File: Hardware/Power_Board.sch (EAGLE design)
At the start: 40 parts, among them K1 E3206S, K2 E3206S, K3 E3206S, K4 E3206S, K5 E3206S, K6 E3206S, Q1 BD135, Q2 BD135, Q3 BD135, Q4 BD135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

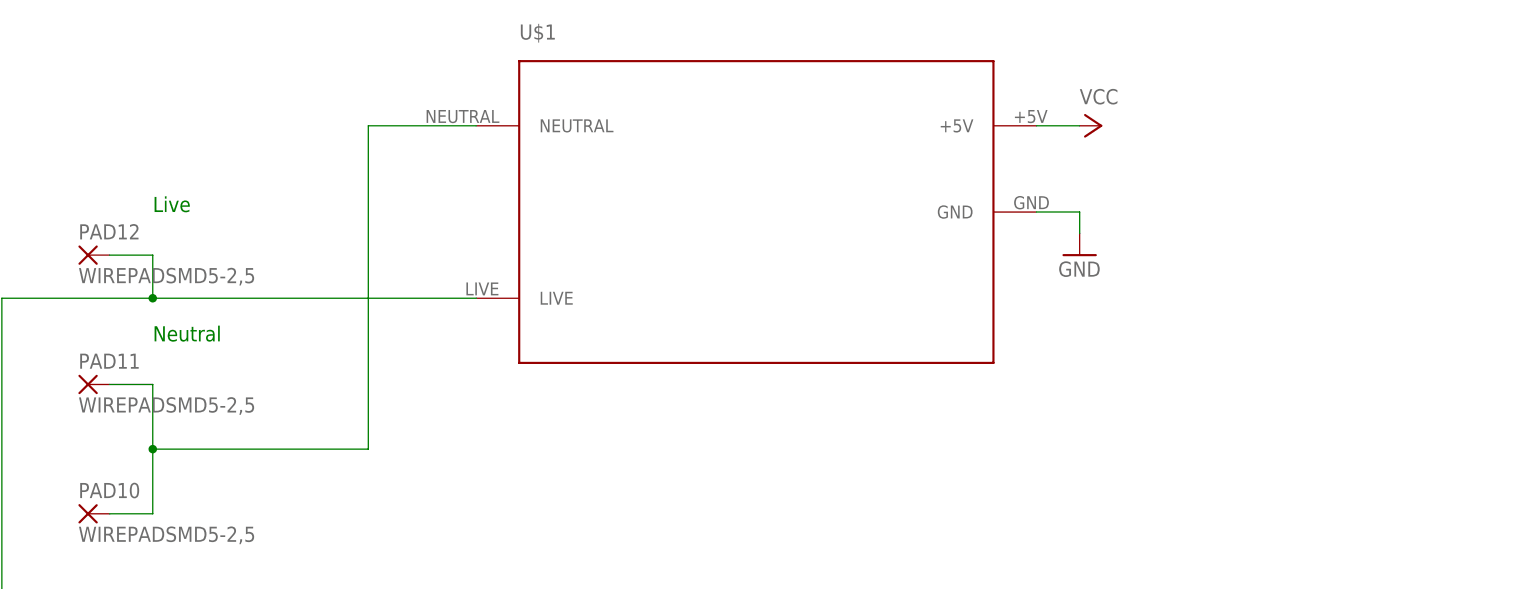
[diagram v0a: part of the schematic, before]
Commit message: Added a fuse to the power board and made PCB routes thicker.
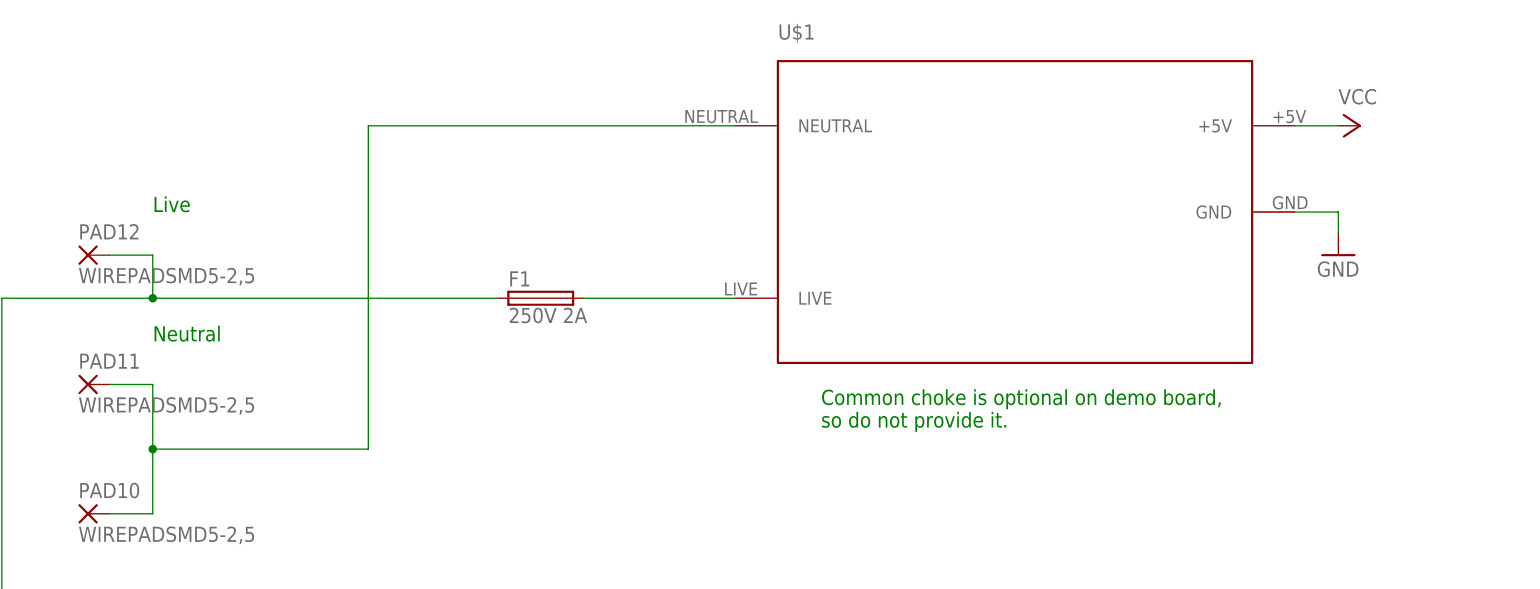
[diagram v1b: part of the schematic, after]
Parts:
- added F1: 250V 2A, fuse:GSH15
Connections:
- new net N$29: F1.2, U$1.LIVE
- net N$10: now also F1.1; no longer U$1.LIVE
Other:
- note added: "Common choke is optional on demo board, so do not provide it."
- moved on the sheet: U$1
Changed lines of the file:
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@@
 <?xml version="1.0" encoding="utf-8"?>
 <!DOCTYPE eagle SYSTEM "eagle.dtd">
-<eagle version="8.3.1">
+<eagle version="8.4.1">
 <drawing>
 <settings>
@@
 <setting verticaltext="down"/>
 </settings>
-<grid distance="0.1" unitdist="inch" unit="inch" style="dots" multiple="1" display="yes" altdistance="0.01" altunitdist="inch" altunit="inch"/>
+<grid distance="0.1" unitdist="inch" unit="inch" style="lines" multiple="1" display="no" altdistance="0.01" altunitdist="inch" altunit="inch"/>
 <layers>
 <layer number="1" name="Top" color="4" fill="1" visible="no" active="no"/>
@@
 <part name="P+1" library="supply1" deviceset="VCC" device=""/>
 <part name="X1" library="con-wago-508" deviceset="W237-02P" device="" value="230V"/>
+<part name="F1" library="fuse" deviceset="GSH15" device="" value="250V 2A"/>
 </parts>
 <sheets>
@@
 <text x="198.12" y="294.64" size="1.778" layer="91">Live</text>
 <text x="180.34" y="294.64" size="1.778" layer="91">Neutral</text>
+<text x="43.18" y="289.56" size="1.778" layer="91">Common choke is optional on demo board,
+so do not provide it.</text>
 </plain>
 <instances>
@@
 <instance part="R5" gate="G$1" x="297.18" y="195.58"/>
 <instance part="R6" gate="G$1" x="297.18" y="165.1"/>
-<instance part="U$1" gate="G$1" x="35.56" y="314.96"/>
-<instance part="GND4" gate="1" x="73.66" y="309.88"/>
-<instance part="P+1" gate="VCC" x="76.2" y="325.12" rot="R270"/>
+<instance part="U$1" gate="G$1" x="66.04" y="314.96"/>
+<instance part="GND4" gate="1" x="104.14" y="309.88"/>
+<instance part="P+1" gate="VCC" x="106.68" y="325.12" rot="R270"/>
 <instance part="X1" gate="-1" x="195.58" y="294.64" smashed="yes" rot="R270">
 <attribute name="NAME" x="196.469" y="295.91" size="1.778" layer="95" rot="R90"/>
@@
 <attribute name="NAME" x="191.389" y="295.91" size="1.778" layer="95" rot="R90"/>
 </instance>
+<instance part="F1" gate="1" x="10.16" y="304.8"/>
 </instances>
 <busses>
@@
 <segment>
 <pinref part="U$1" gate="G$1" pin="GND"/>
-<wire x1="68.58" y1="314.96" x2="73.66" y2="314.96" width="0.1524" layer="91"/>
+<wire x1="99.06" y1="314.96" x2="104.14" y2="314.96" width="0.1524" layer="91"/>
 <pinref part="GND4" gate="1" pin="GND"/>
-<wire x1="73.66" y1="314.96" x2="73.66" y2="312.42" width="0.1524" layer="91"/>
+<wire x1="104.14" y1="314.96" x2="104.14" y2="312.42" width="0.1524" layer="91"/>
 </segment>
 </net>
@@
 <pinref part="U$1" gate="G$1" pin="+5V"/>
 <pinref part="P+1" gate="VCC" pin="VCC"/>
-<wire x1="68.58" y1="325.12" x2="73.66" y2="325.12" width="0.1524" layer="91"/>
+<wire x1="99.06" y1="325.12" x2="104.14" y2="325.12" width="0.1524" layer="91"/>
 </segment>
 </net>
@@
 <wire x1="-5.08" y1="243.84" x2="-53.34" y2="243.84" width="0.1524" layer="91"/>
 <junction x="-53.34" y="243.84"/>
-<wire x1="-35.56" y1="304.8" x2="2.54" y2="304.8" width="0.1524" layer="91"/>
+<pinref part="F1" gate="1" pin="1"/>
+<wire x1="-35.56" y1="304.8" x2="5.08" y2="304.8" width="0.1524" layer="91"/>
 <junction x="-35.56" y="304.8"/>
-<pinref part="U$1" gate="G$1" pin="LIVE"/>
 </segment>
 </net>
@@
 <segment>
 <pinref part="U$1" gate="G$1" pin="NEUTRAL"/>
-<wire x1="-10.16" y1="325.12" x2="2.54" y2="325.12" width="0.1524" layer="91"/>
+<wire x1="-10.16" y1="325.12" x2="33.02" y2="325.12" width="0.1524" layer="91"/>
 <wire x1="-10.16" y1="287.02" x2="-10.16" y2="325.12" width="0.1524" layer="91"/>
 <pinref part="PAD10" gate="G$1" pin="P"/>
@@
 </segment>
 </net>
+<net name="N$29" class="1">
+<segment>
+<pinref part="F1" gate="1" pin="2"/>
+<pinref part="U$1" gate="G$1" pin="LIVE"/>
+<wire x1="15.24" y1="304.8" x2="33.02" y2="304.8" width="0.1524" layer="91"/>
+</segment>
+</net>
 </nets>
 </sheet>
@@
 </schematic>
 </drawing>
+<compatibility>
+<note version="6.3" minversion="6.2.2" severity="warning">
+Since Version 6.2.2 text objects can contain more than one line,
+which will not be processed correctly with this version.
+</note>
+</compatibility>
 </eagle>

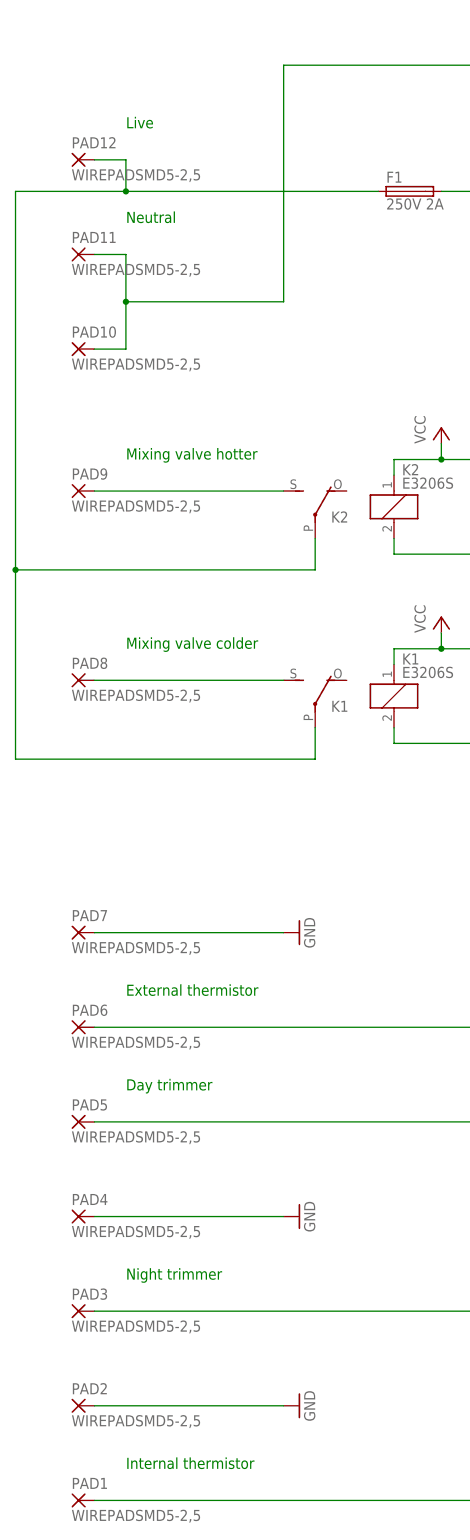
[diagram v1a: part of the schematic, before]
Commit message: Added bigger pads to the power board PCB, so the PCB coating won't recover the pads.
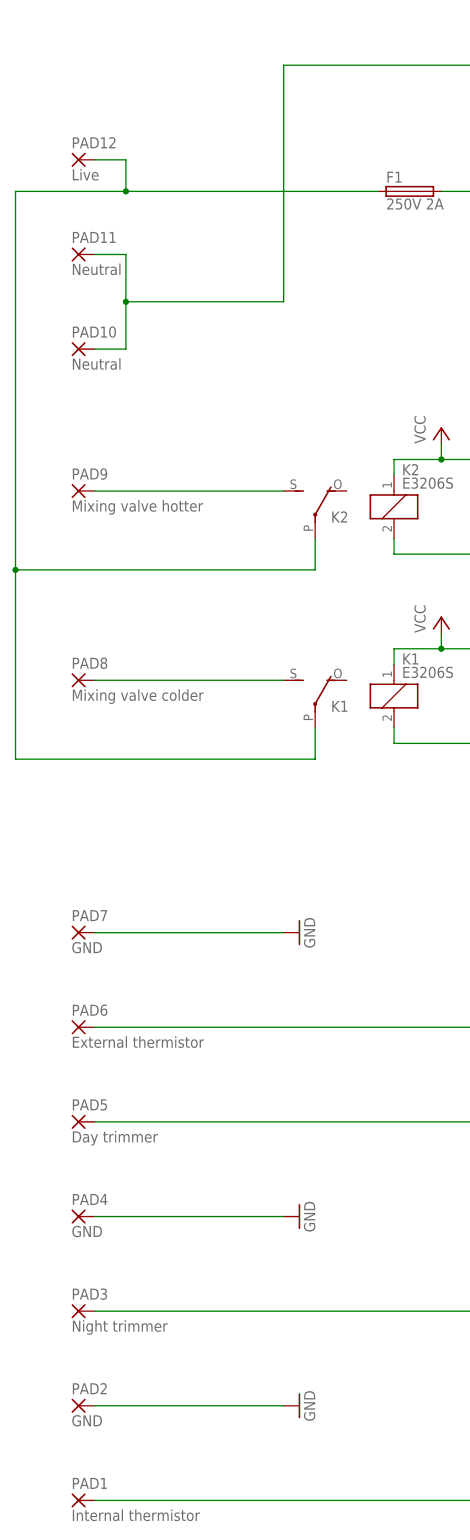
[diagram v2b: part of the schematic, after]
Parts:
- PAD1: value WIREPADSMD5-2,5 -> Internal thermistor; device wirepad:WIREPADSMD5-2,5 -> Pad:SMD20
- PAD10, PAD11: value WIREPADSMD5-2,5 -> Neutral; device wirepad:WIREPADSMD5-2,5 -> Pad:SMD20
- PAD12: value WIREPADSMD5-2,5 -> Live; device wirepad:WIREPADSMD5-2,5 -> Pad:SMD20
- PAD2, PAD4, PAD7: value WIREPADSMD5-2,5 -> GND; device wirepad:WIREPADSMD5-2,5 -> Pad:SMD20
- PAD3: value WIREPADSMD5-2,5 -> Night trimmer; device wirepad:WIREPADSMD5-2,5 -> Pad:SMD20
- PAD5: value WIREPADSMD5-2,5 -> Day trimmer; device wirepad:WIREPADSMD5-2,5 -> Pad:SMD20
- PAD6: value WIREPADSMD5-2,5 -> External thermistor; device wirepad:WIREPADSMD5-2,5 -> Pad:SMD20
- PAD8: value WIREPADSMD5-2,5 -> Mixing valve colder; device wirepad:WIREPADSMD5-2,5 -> Pad:SMD20
- PAD9: value WIREPADSMD5-2,5 -> Mixing valve hotter; device wirepad:WIREPADSMD5-2,5 -> Pad:SMD20
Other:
- note removed: "Day trimmer"
- note removed: "External thermistor"
- note removed: "Internal thermistor"
- note removed: "Mixing valve colder"
- note removed: "Mixing valve hotter"
- note removed: "Night trimmer"
